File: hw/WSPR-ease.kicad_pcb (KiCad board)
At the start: 4 copper layers, 99 x 64 mm, 137 parts, among them J101 SMA, J102 SMA, J103 pwr+data, Q101 MMBF170, Q301 MMBF170, Q302 MMBF170, Q303 MMBF170, Q304 MMBF170, Q305 MMBF170, Q306 MMBF170, Q307 MMBF170, Q308 MMBF170, Q309 MMBF170, Q310 MMBF170, Q311 MMBF170, Q312 MMBF170, T301 BN-43-202_DualPri_CTSec, U101 GNSS module, U102 ESP32-S3-WROOM-1-N8R8, U103 SRV05-4, U104 TPS22918DBVR, U105 TPS74612PQWDRBRQ1, U106 LMR51430YDDCR, U201 AS183-92LF, U202 AS183-92LF, U203 AS183-92LF, U204 AS183-92LF, U301 ICE40UP5K-SG48ITR, U302 CD74ACT541SM96, Y301 40MHz

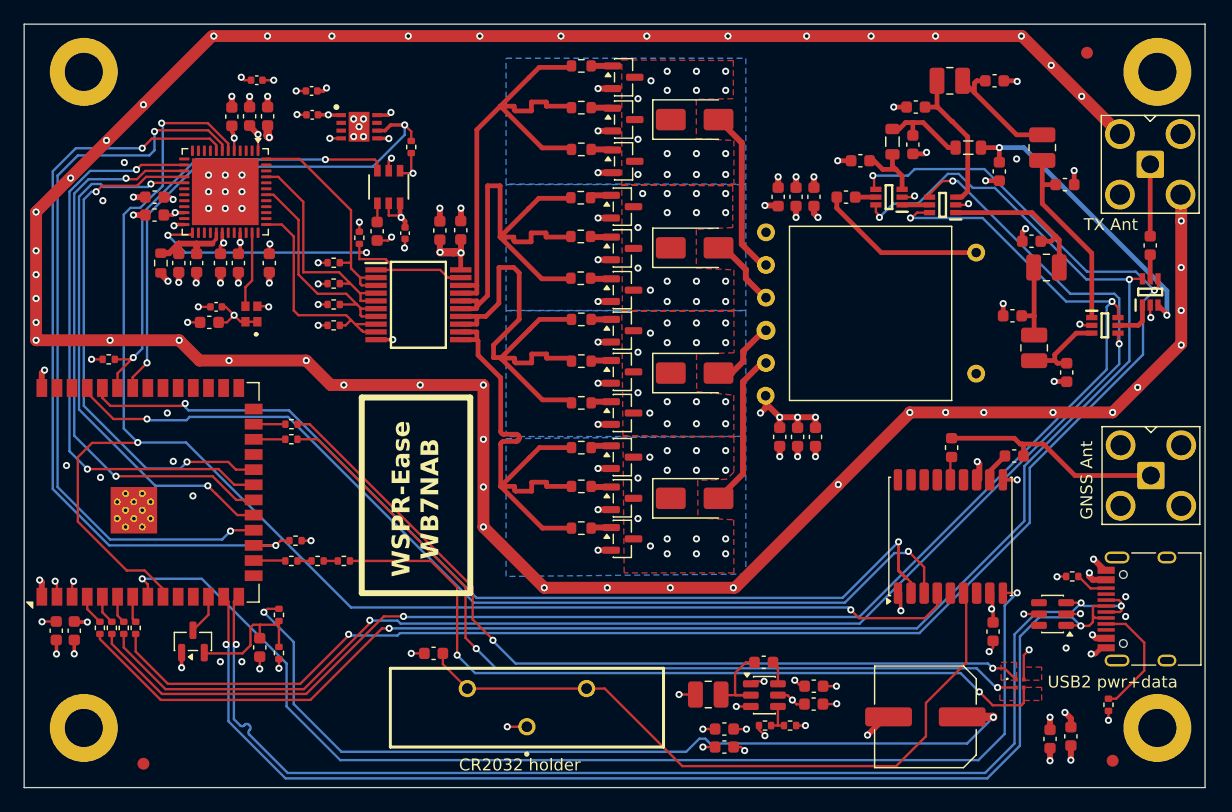
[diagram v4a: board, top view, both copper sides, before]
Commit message: Separate FPGA config CRESET from software NRESET, add RGB heartbeat to FPGA.
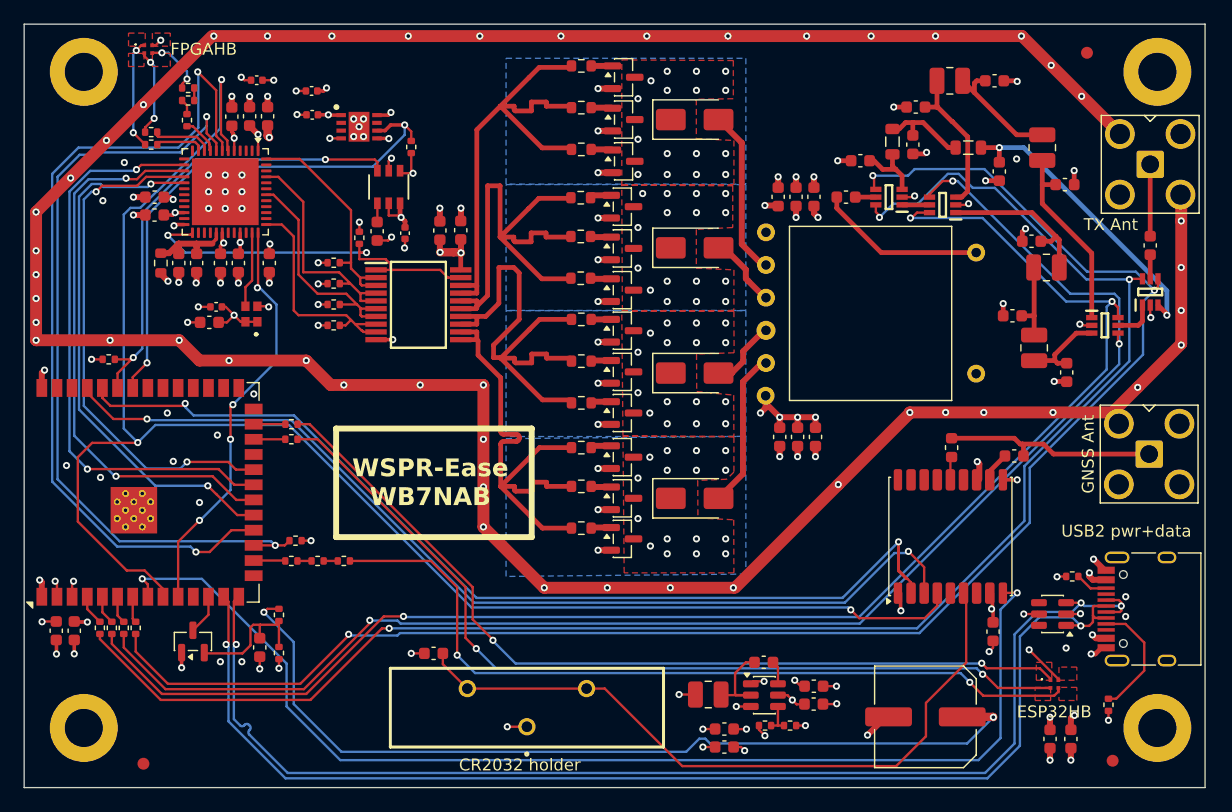
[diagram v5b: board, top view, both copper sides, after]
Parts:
- added D301: LED_BGRA, Library:UHD111AFKAC3K23E1L3VG5ZB3Z3, F.Cu at (60.0, 71.5)
- added R316: 100, Resistor_SMD:R_0402_1005Metric, F.Cu at (63.2, 77.5)
- added R317: 100, Resistor_SMD:R_0402_1005Metric, F.Cu at (63.4, 75.8)
- added R318: 100, Resistor_SMD:R_0402_1005Metric, F.Cu at (60.2, 78.5)
- added R319: 100, Resistor_SMD:R_0402_1005Metric, F.Cu at (60.2, 79.5)
- added R323: 100, Resistor_SMD:R_0402_1005Metric, F.Cu at (63.4, 74.8)
- moved D101 2.90 mm to (136.0, 124.7)
- moved J101 1.81 mm to (143.9, 105.4)
- moved C111 0.22 mm to (137.3, 129.3)
- renumbered C305 to C301, C306 to C302, C301 to C303, C302 to C304, C307 to C305, C310 to C306, C308 to C307, C309 to C308, C311 to C309, C312 to C310, C303 to C311, C304 to C312, C320 to C313, C313 to C314, C314 to C315, C315 to C316, C318 to C317, C317 to C318, C316 to C319, C319 to C320, D301 to D302, D302 to D303, D303 to D304, D304 to D305, R117 to R108, R116 to R109, R108 to R110, R109 to R111, R110 to R112, R111 to R113, R112 to R114, R113 to R115, R114 to R116, R115 to R117, R319 to R306, R306 to R307, R307 to R308, R308 to R309, R309 to R310, R310 to R311, R311 to R312, R312 to R313, R313 to R314, R314 to R315, R315 to R320, R316 to R321, R317 to R322, R318 to R324, U105 to U104, U104 to U105
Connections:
- R301 pad 1: /fpgaNRESET -> /fpgaCRESET
- U102 pad 10: unconnected-(U102-IO17-Pad10) -> /fpgaNRESET
- U102 pad 17: /fpgaNRESET -> /fpgaCRESET
- U301 pad 10: unconnected-(U301B-IOB_18a-Pad10) -> /Transmitter/hbG
- U301 pad 11: unconnected-(U301B-IOB_20a-Pad11) -> /Transmitter/hbB
- U301 pad 36: unconnected-(U301A-IOT_48b-Pad36) -> /fpgaNRESET
- U301 pad 8: /fpgaNRESET -> /fpgaCRESET
- U301 pad 9: unconnected-(U301B-IOB_16a-Pad9) -> /Transmitter/hbR
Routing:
- net /fpgaCRESET: track 0.00 -> 67.3 mm, vias 0 -> 2
- net /fpgaNRESET: track 66.0 -> 34.8 mm, vias 2 -> 4
- net /fpgaDONE: track 62.0 -> 71.9 mm
- net /Transmitter/blu: track 0.00 -> 9.25 mm, vias 0 -> 2
- net /Transmitter/grn: track 0.00 -> 7.28 mm, vias 0 -> 2
- net /gnssPPS: track 131.7 -> 138.0 mm
- net /Transmitter/red: track 0.00 -> 5.10 mm, vias 0 -> 2
- net /Transmitter/hbG: track 0.00 -> 5.09 mm
- net /Transmitter/hbB: track 0.00 -> 4.11 mm
- net /Transmitter/hbR: track 0.00 -> 3.15 mm
- net /blu: track 70.7 -> 73.7 mm
- net /grn: track 71.2 -> 74.1 mm
- net +3.3V: track 26.2 -> 27.9 mm, vias 17 -> 18
- net /red: track 66.2 -> 67.9 mm
- net Net-(R316-Pad2): track 0.00 -> 1.31 mm
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- added copper zone on F.Cu, net /Transmitter/blu
- added copper zone on F.Cu, net /Transmitter/grn
- added copper zone on F.Cu, net /Transmitter/red

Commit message: Move to single gate buffer per MOSFET to distribute decoupling and gate drive across more devices and improve gate drive signal quality at high speed
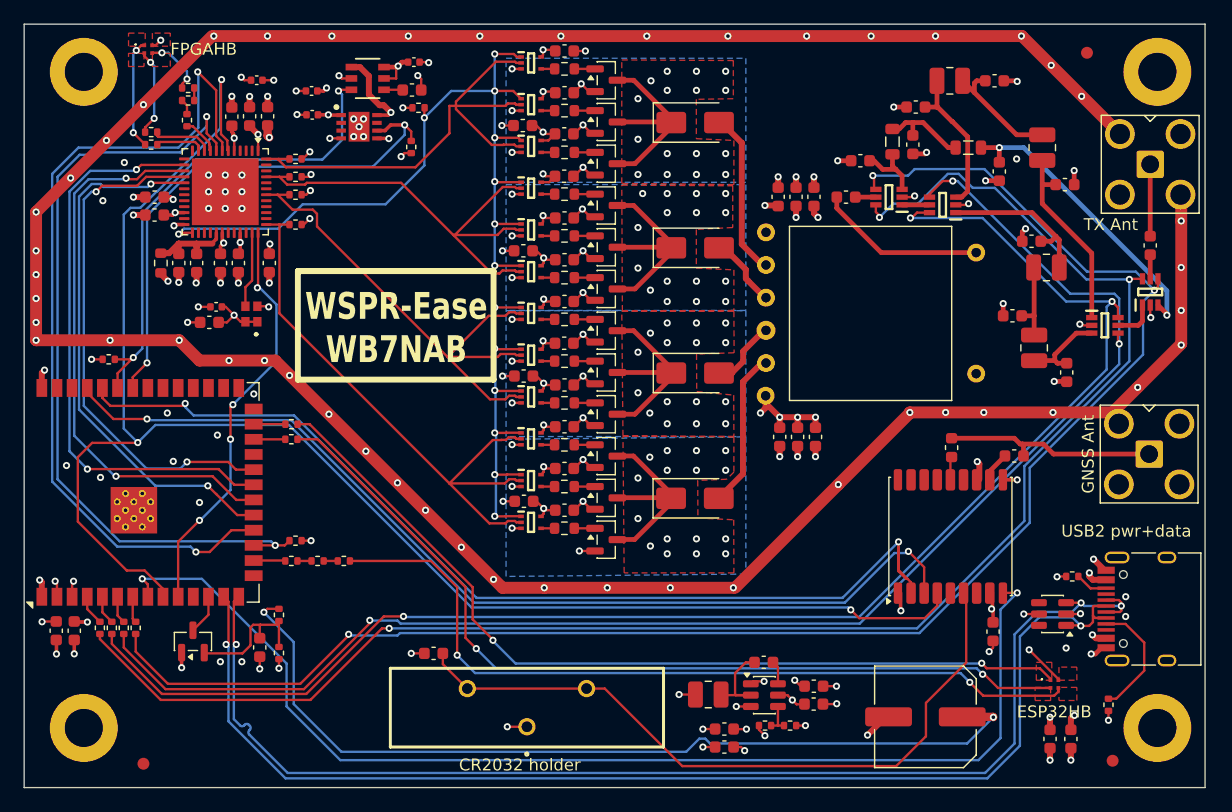
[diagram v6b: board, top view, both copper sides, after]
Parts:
- removed D302, D303, D304, D305: SS14, Diode_SMD:D_SMA
- removed Q301, Q302, Q303, Q304, Q305, Q306, Q307, Q308, Q309, Q310, Q311, Q312: MMBF170, Package_TO_SOT_SMD:SOT-23
- removed the R307 at (96.3, 94.2)
- removed the R308 at (96.3, 97.7)
- removed the R309 at (96.3, 101.2)
- removed the R310 at (96.3, 104.9)
- removed the R311 at (96.3, 108.2)
- removed the R312 at (96.3, 111.7)
- removed R313, R314, R315, R320, R321, R322: 10, Resistor_SMD:R_0603_1608Metric
- removed U302: CD74ACT541SM96, Library:SOP65P780X200-20N
- added C309: 10uF X5R 25V, Capacitor_SMD:C_0603_1608Metric, F.Cu at (91.4, 77.9)
- added C310: 10uF X5R 25V, Capacitor_SMD:C_0603_1608Metric, F.Cu at (91.5, 98.9)
- added C401: 100nF X7R 50V, Capacitor_SMD:C_0603_1608Metric, F.Cu at (94.9, 96.2)
- added C402: 100nF X7R 50V, Capacitor_SMD:C_0603_1608Metric, F.Cu at (94.9, 92.7)
- added C403: 100nF X7R 50V, Capacitor_SMD:C_0603_1608Metric, F.Cu at (94.9, 99.7)
- added C501: 100nF X7R 50V, Capacitor_SMD:C_0603_1608Metric, F.Cu at (94.9, 106.7)
- added C502: 100nF X7R 50V, Capacitor_SMD:C_0603_1608Metric, F.Cu at (94.9, 103.2)
- added C503: 100nF X7R 50V, Capacitor_SMD:C_0603_1608Metric, F.Cu at (94.9, 110.2)
- added C601: 100nF X7R 50V, Capacitor_SMD:C_0603_1608Metric, F.Cu at (94.9, 85.7)
- added C602: 100nF X7R 50V, Capacitor_SMD:C_0603_1608Metric, F.Cu at (94.9, 82.2)
- added C603: 100nF X7R 50V, Capacitor_SMD:C_0603_1608Metric, F.Cu at (94.9, 89.2)
- added C701: 100nF X7R 50V, Capacitor_SMD:C_0603_1608Metric, F.Cu at (94.9, 75.2)
- added C702: 100nF X7R 50V, Capacitor_SMD:C_0603_1608Metric, F.Cu at (94.9, 71.7)
- added C703: 100nF X7R 50V, Capacitor_SMD:C_0603_1608Metric, F.Cu at (94.9, 78.6)
- added D401: SS14, Diode_SMD:D_SMA, F.Cu at (105.8, 98.7)
- added D501: SS14, Diode_SMD:D_SMA, F.Cu at (105.8, 109.2)
- added D601: SS14, Diode_SMD:D_SMA, F.Cu at (105.8, 88.2)
- added D701: SS14, Diode_SMD:D_SMA, F.Cu at (105.8, 77.7)
- added IC401: SN74AHCT1G125DRLR, Library:SOTFL50P160X60-5N, F.Cu at (92.1, 97.2)
- added IC402: SN74AHCT1G125DRLR, Library:SOTFL50P160X60-5N, F.Cu at (92.1, 93.7)
- added IC403: SN74AHCT1G125DRLR, Library:SOTFL50P160X60-5N, F.Cu at (92.1, 100.7)
- added IC501: SN74AHCT1G125DRLR, Library:SOTFL50P160X60-5N, F.Cu at (92.1, 107.7)
- added IC502: SN74AHCT1G125DRLR, Library:SOTFL50P160X60-5N, F.Cu at (92.1, 104.2)
- added IC503: SN74AHCT1G125DRLR, Library:SOTFL50P160X60-5N, F.Cu at (92.1, 111.2)
- added IC601: SN74AHCT1G125DRLR, Library:SOTFL50P160X60-5N, F.Cu at (92.1, 86.7)
- added IC602: SN74AHCT1G125DRLR, Library:SOTFL50P160X60-5N, F.Cu at (92.1, 83.2)
- added IC603: SN74AHCT1G125DRLR, Library:SOTFL50P160X60-5N, F.Cu at (92.1, 90.2)
- added IC701: SN74AHCT1G125DRLR, Library:SOTFL50P160X60-5N, F.Cu at (92.1, 76.2)
- added IC702: SN74AHCT1G125DRLR, Library:SOTFL50P160X60-5N, F.Cu at (92.1, 72.7)
- added IC703: SN74AHCT1G125DRLR, Library:SOTFL50P160X60-5N, F.Cu at (92.1, 79.7)
- added Q401: MMBF170, Package_TO_SOT_SMD:SOT-23, F.Cu at (98.4, 95.1)
- added Q402: MMBF170, Package_TO_SOT_SMD:SOT-23, F.Cu at (98.4, 98.6)
- added Q403: MMBF170, Package_TO_SOT_SMD:SOT-23, F.Cu at (98.4, 102.1)
- added Q501: MMBF170, Package_TO_SOT_SMD:SOT-23, F.Cu at (98.4, 105.6)
- added Q502: MMBF170, Package_TO_SOT_SMD:SOT-23, F.Cu at (98.4, 109.1)
- added Q503: MMBF170, Package_TO_SOT_SMD:SOT-23, F.Cu at (98.4, 112.6)
- added Q601: MMBF170, Package_TO_SOT_SMD:SOT-23, F.Cu at (98.4, 84.6)
- added Q602: MMBF170, Package_TO_SOT_SMD:SOT-23, F.Cu at (98.4, 88.1)
- added Q603: MMBF170, Package_TO_SOT_SMD:SOT-23, F.Cu at (98.4, 91.6)
- added Q701: MMBF170, Package_TO_SOT_SMD:SOT-23, F.Cu at (98.4, 74.1)
- added Q702: MMBF170, Package_TO_SOT_SMD:SOT-23, F.Cu at (98.4, 77.6)
- added Q703: MMBF170, Package_TO_SOT_SMD:SOT-23, F.Cu at (98.4, 81.1)
- added R401: 10, Resistor_SMD:R_0603_1608Metric, F.Cu at (94.9, 94.2)
- added R402: 10, Resistor_SMD:R_0603_1608Metric, F.Cu at (94.9, 97.7)
- added R403: 10, Resistor_SMD:R_0603_1608Metric, F.Cu at (94.9, 101.2)
- added R501: 10, Resistor_SMD:R_0603_1608Metric, F.Cu at (94.9, 104.7)
- added R502: 10, Resistor_SMD:R_0603_1608Metric, F.Cu at (94.9, 108.2)
- added R503: 10, Resistor_SMD:R_0603_1608Metric, F.Cu at (94.9, 111.7)
- added R601: 10, Resistor_SMD:R_0603_1608Metric, F.Cu at (94.9, 83.7)
- added R602: 10, Resistor_SMD:R_0603_1608Metric, F.Cu at (94.9, 87.2)
- added R603: 10, Resistor_SMD:R_0603_1608Metric, F.Cu at (94.9, 90.7)
- added R701: 10, Resistor_SMD:R_0603_1608Metric, F.Cu at (94.9, 73.2)
- added R702: 10, Resistor_SMD:R_0603_1608Metric, F.Cu at (94.9, 76.7)
- added R703: 10, Resistor_SMD:R_0603_1608Metric, F.Cu at (94.9, 80.2)
- C308: value 100nF X7R 50V -> 10uF X5R 25V
- moved C308 23.3 mm to (91.5, 109.4), turned to 0 degrees
- moved C109 14.4 mm to (82.3, 72.6), turned to 0 degrees
- moved C107 12.2 mm to (82.1, 74.9), turned to 0 degrees
- moved R306 12.0 mm to (82.7, 76.4), turned to 180 degrees
- moved R310 9.74 mm to (72.3, 83.7), turned to 0 degrees
- moved R308 9.50 mm to (72.3, 82.2), turned to 0 degrees
- moved R309 9.27 mm to (72.3, 80.7), turned to 0 degrees
- moved U105 9.27 mm to (78.4, 74.0), turned to 0 degrees
- moved R311 9.04 mm to (72.3, 86.2), turned to 0 degrees
- moved C307 7.20 mm to (91.5, 88.4), turned to 0 degrees
- renumbered C309 to C305, C310 to C306, C305 to C320, C320 to C321, C321 to C322, C322 to C323, C306 to C324, J103 to J102, J102 to J103, R316 to R301, R317 to R302, R318 to R303, R319 to R304, R323 to R305, R301 to R307, R302 to R308, R303 to R309, R304 to R310, R305 to R311, R324 to R312
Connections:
- C307 pad 2: +VFPGAIO -> VBUS
- C308 pad 2: +VFPGAIO -> VBUS
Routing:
- net /Transmitter/driverNEN: track 31.9 -> 101.3 mm, vias 2 -> 14
- net /Transmitter/pull2G: track 41.3 -> 0.00 mm
- net /Transmitter/push1G: track 41.2 -> 0.00 mm
- net /Transmitter/pull1G: track 41.2 -> 0.00 mm
- net /Transmitter/push2G: track 41.2 -> 0.00 mm
- net /Transmitter/push2: track 19.4 -> 50.9 mm
- net VBUS: track 97.0 -> 123.3 mm, vias 16 -> 28
- net /Transmitter/push1: track 19.2 -> 44.3 mm
- net /Transmitter/pull2: track 19.0 -> 40.5 mm
- net /Transmitter/pull1: track 19.5 -> 39.0 mm
- net /Transmitter/push2D: track 0.00 -> 16.1 mm
- net /Transmitter/push1D: track 0.00 -> 16.1 mm
- net /Transmitter/pull2D: track 0.00 -> 16.1 mm
- net /Transmitter/pull1D: track 0.00 -> 16.1 mm
- net GND: track 335.1 -> 348.6 mm, vias 162 -> 177
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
